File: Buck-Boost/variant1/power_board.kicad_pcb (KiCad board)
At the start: 2 copper layers, 108 x 42 mm, 25 parts, among them J1 Conn_01x05_Header, Q1 NMOS, Vds>=80V, Rds<=1.5mOhm, Q2 NMOS, Vds>=80V, Rds<=1.5mOhm, Q3 NMOS, Vds>=80V, Rds<=1.5mOhm, Q4 NMOS, Vds>=80V, Rds<=1.5mOhm, Q5 NMOS, Vds>=80V, Rds<=1.5mOhm, Q6 NMOS, Vds>=80V, Rds<=1.5mOhm, Q7 NMOS, Vds>=80V, Rds<=1.5mOhm, Q8 NMOS, Vds>=80V, Rds<=1.5mOhm

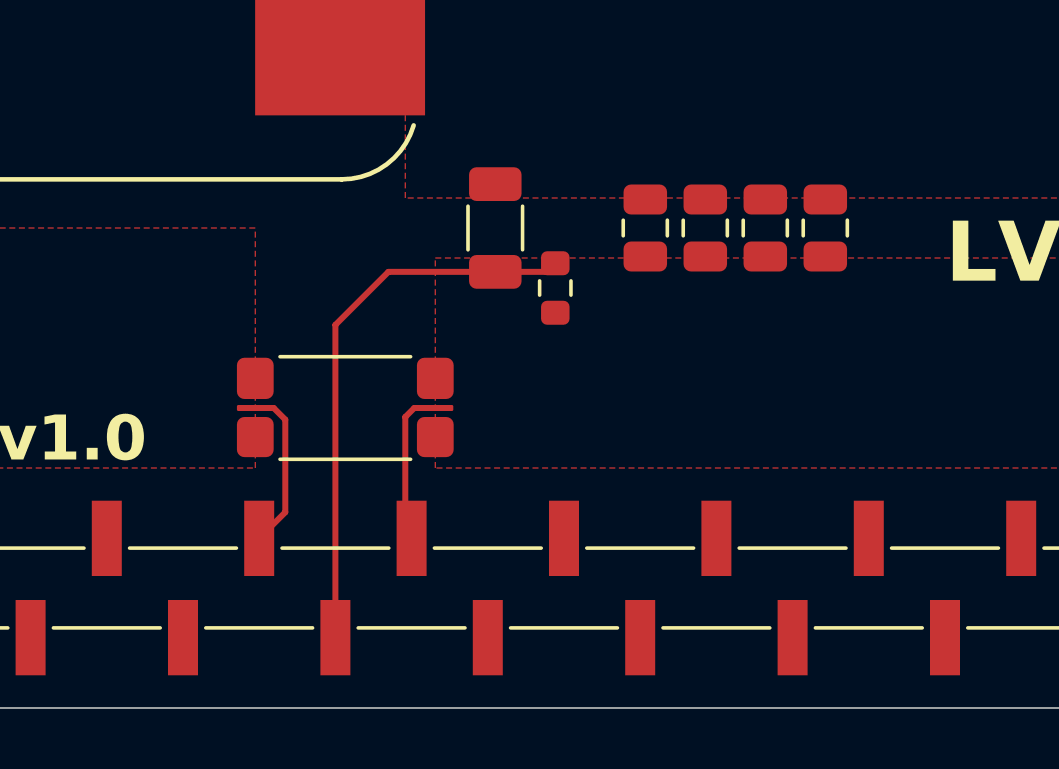
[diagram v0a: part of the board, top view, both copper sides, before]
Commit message: buck-boost/control & buck-boost/variant1 - corrected the pin-config
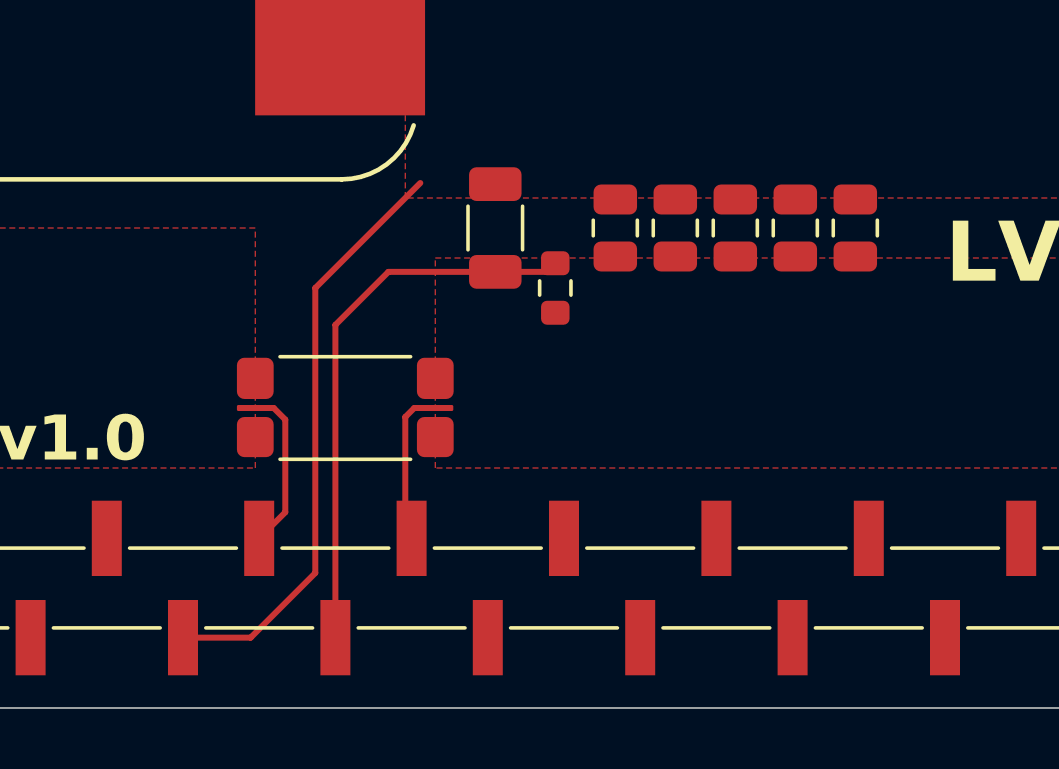
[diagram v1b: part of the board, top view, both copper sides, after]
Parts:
- added C2: >22uF, >25V, Capacitor_SMD:C_0805_2012Metric, F.Cu at (164.0, 73.0)
- R18: value 1mOhm, >=3W -> 500uOhm, >=3W
- moved C10 1.00 mm to (166.0, 73.0)
- moved C4 1.00 mm to (172.0, 73.0)
- moved C8 1.00 mm to (170.0, 73.0)
- moved C9 1.00 mm to (168.0, 73.0)
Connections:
- net /HV+ renamed HV+
- C10 pad 1: /LV+ -> LV+
- C4 pad 1: /LV+ -> LV+
- C8 pad 1: /LV+ -> LV+
- C9 pad 1: /LV+ -> LV+
- J1 pad 12: Iin_+ -> I_hv_+
- J1 pad 29: unconnected-(J1-Pin_29-Pad29) -> LV+
- J1 pad 30: Iout_- -> I_lv_-
- J1 pad 32: Iout_+ -> I_lv_+
- J1 pad 6: Iin_- -> I_hv_-
- L1 pad 1: /LV+ -> LV+
- R11 pad 1: /LV+ -> LV+
- R18 pad 2: Iin_- -> /Iin_-
- R18 pad 3: Iin_+ -> /Iin_+
- R5 pad 2: Iout_- -> /Iout_-
- R5 pad 3: Iout_+ -> /Iout_+
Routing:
- net (no net): track 0.00 -> 33.5 mm
- net LV+: track 0.00 -> 19.8 mm
- net Iin_+: track 15.3 -> 0.00 mm
- net Iin_-: track 7.46 -> 0.00 mm
- net Iout_-: track 5.48 -> 0.00 mm
- net Iout_+: track 5.25 -> 0.00 mm
- added copper zone on F.Cu, net LV+
- removed copper zone on F.Cu, net /LV+
